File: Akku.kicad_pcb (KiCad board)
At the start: 2 copper layers, 100 x 160 mm, 49 parts, among them P1 CONN_02X10, P2 CONN_02X10, P3 CONN_02X10, P4 CONN_01X01, P5 CONN_01X01, P6 CONN_01X01, P7 CONN_01X01, P8 CONN_01X01, P9 CONN_01X01, SW1 SWITCH_INV, SW2 SWITCH_INV, SW3 SWITCH_INV, U1 7400, U2 7408, U3 74HC14, U4 74LS193, U5 74LS541, U6 74LS193, U7 74LS540, U8 74HC14

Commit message: Todo list dabei
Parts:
- removed REF**: EuroBoard160mmX100mm_holes, EuroBoard_Outline:EuroBoard160mmX100mm_holes
- added P10: CONN_01X01, Connect:1pin, F.Cu at (166.3, 60.7)
- added P11: CONN_01X01, Connect:1pin, F.Cu at (176.5, 60.7)
- P1, P2, P3: value CONN_02X10 -> CONN_01X01; footprint Connect:IDC_Header_Straight_20pins -> Connect:1pin
- P7, P8, P9: value CONN_01X01 -> CONN_02X10
- SW1: value SWITCH_INV -> UP_Bonsai_SWITCH_INV
- SW2: value SWITCH_INV -> DOWN_Bonsai_SWITCH_INV
- SW3: value SWITCH_INV -> CLR_Bonsai_SWITCH_INV
- U1: value 7400 -> 74HC14; footprint Housings_DIP:DIP-14_W7.62mm -> Housings_DIP:DIP-14_W7.62mm_LongPads
- U2: value 7408 -> 7400; footprint Housings_DIP:DIP-14_W7.62mm -> Housings_DIP:DIP-14_W7.62mm_LongPads
- U4: value 74LS193 -> 7408; footprint Housings_DIP:DIP-16_W7.62mm_LongPads -> Housings_DIP:DIP-14_W7.62mm_LongPads
- U5: value 74LS541 -> 74LS193; footprint Housings_DIP:DIP-20_W7.62mm_LongPads -> Housings_DIP:DIP-16_W7.62mm_LongPads
- U6: value 74LS193 -> 74LS541; footprint Housings_DIP:DIP-16_W7.62mm_LongPads -> Housings_DIP:DIP-20_W7.62mm_LongPads
- U7: value 74LS540 -> 74LS193; footprint Housings_DIP:DIP-20_W7.62mm_LongPads -> Housings_DIP:DIP-16_W7.62mm_LongPads
- U8: value 74HC14 -> 74LS540; footprint Housings_DIP:DIP-14_W7.62mm_LongPads -> Housings_DIP:DIP-20_W7.62mm_LongPads
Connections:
- D1 pad 1: GND -> Net-(D1-Pad1)
- D3 pad 1: Net-(D3-Pad1) -> GND
- P1 pad 1: GND -> enable
- P2 pad 1: GND -> up
- P3 pad 1: GND -> down
- P4 pad 1: down/up/enable/load/CLR -> CLR
- P6 pad 1: down/up/enable/load/CLR -> load
- P7 pad 1: down/up/enable/load/CLR -> Net-(P7-Pad1)
- P8 pad 1: down/up/enable/load/CLR -> Net-(P8-Pad1)
- P9 pad 1: down/up/enable/load/CLR -> GND
- R1 pad 2: Net-(R1-Pad2) -> up
- R10 pad 2: Net-(D1-Pad2) -> Net-(D2-Pad2)
- R11 pad 2: Net-(D2-Pad2) -> Net-(D3-Pad2)
- R5 pad 2: up -> Net-(R5-Pad2)
- R6 pad 1: VCC -> Net-(R6-Pad1)
- R6 pad 2: down -> VCC
- R9 pad 1: Net-(D3-Pad1) -> Net-(D1-Pad1)
- SW1 pad 1: Net-(SW1-Pad1) -> Net-(R4-Pad2)
- SW2 pad 1: Net-(R4-Pad2) -> Net-(R7-Pad2)
- U1 pad 1: Net-(R1-Pad2) -> enable
- U1 pad 10: Net-(R3-Pad1) -> (no net)
- U1 pad 11: Net-(U1-Pad11) -> (no net)
- U1 pad 12: Net-(R4-Pad2) -> (no net)
- U1 pad 13: Net-(U1-Pad13) -> (no net)
- U1 pad 4: Net-(U1-Pad4) -> Net-(R10-Pad1)
- U1 pad 5: Net-(R2-Pad2) -> Net-(U1-Pad5)
- U1 pad 6: Net-(U1-Pad6) -> Net-(D1-Pad2)
- U1 pad 8: Net-(U1-Pad13) -> Net-(R14-Pad1)
- U1 pad 9: Net-(U1-Pad11) -> load
- U2 pad 1: up -> Net-(R4-Pad2)
- U2 pad 10: (no net) -> Net-(R6-Pad1)
- U2 pad 12: Net-(U1-Pad13) -> Net-(R7-Pad2)
- U2 pad 13: down -> Net-(U2-Pad13)
- U2 pad 2: Net-(U1-Pad3) -> Net-(U2-Pad2)
- U2 pad 4: (no net) -> Net-(U2-Pad3)
- U2 pad 5: (no net) -> Net-(R5-Pad2)
- U2 pad 6: (no net) -> Net-(U2-Pad2)
- U2 pad 8: (no net) -> Net-(U2-Pad13)
- U2 pad 9: (no net) -> Net-(U2-Pad11)
- U3 pad 14: VDD -> VCC
- U3 pad 3: Net-(U3-Pad3) -> Net-(U1-Pad2)
- U3 pad 4: Net-(U3-Pad4) -> Net-(U1-Pad5)
- U3 pad 5: Net-(U2-Pad3) -> Net-(U3-Pad5)
- U3 pad 6: Net-(R10-Pad1) -> Net-(R11-Pad1)
- U3 pad 7: VSS -> GND
- U4 pad 1: Net-(U4-Pad1) -> up
- U4 pad 10: Net-(U4-Pad10) -> (no net)
- U4 pad 11: load -> Net-(U1-Pad3)
- U4 pad 12: Net-(U4-Pad12) -> Net-(U2-Pad13)
- U4 pad 13: Net-(U4-Pad13) -> down
- U4 pad 14: CLR -> VCC
- U4 pad 2: Net-(U4-Pad2) -> Net-(U2-Pad3)
- U4 pad 3: Net-(U4-Pad3) -> Net-(U3-Pad5)
- U4 pad 4: Net-(U2-Pad11) -> (no net)
- U4 pad 5: Net-(U4-Pad5) -> (no net)
- U4 pad 6: Net-(U4-Pad6) -> (no net)
- U4 pad 7: Net-(U4-Pad7) -> GND
- U4 pad 8: GND -> (no net)
- U4 pad 9: Net-(U4-Pad9) -> (no net)
- U5 pad 10: GND -> Net-(U5-Pad10)
- U5 pad 11: Net-(U5-Pad11) -> load
- U5 pad 14: Net-(U5-Pad14) -> CLR
- U5 pad 15: Net-(U4-Pad9) -> Net-(U5-Pad15)
- U5 pad 16: Net-(U4-Pad10) -> VCC
- U5 pad 2: Net-(U4-Pad2) -> Net-(U5-Pad2)
- U5 pad 3: Net-(U4-Pad3) -> Net-(U5-Pad3)
- U5 pad 4: Net-(U4-Pad7) -> Net-(U1-Pad3)
- U5 pad 5: Net-(U4-Pad6) -> Net-(U3-Pad5)
- U5 pad 8: Net-(U5-Pad8) -> GND
- U6 pad 1: Net-(U5-Pad13) -> Net-(U1-Pad5)
- U6 pad 10: Net-(U5-Pad12) -> GND
- U6 pad 11: load -> Net-(U6-Pad11)
- U6 pad 14: CLR -> Net-(U6-Pad14)
- U6 pad 15: Net-(U5-Pad14) -> Net-(U5-Pad9)
- U6 pad 16: VCC -> Net-(U5-Pad10)
- U6 pad 2: Net-(U5-Pad6) -> Net-(U5-Pad2)
- U6 pad 3: Net-(U5-Pad7) -> Net-(U5-Pad3)
- U6 pad 4: Net-(U4-Pad13) -> Net-(U5-Pad7)
- U6 pad 5: Net-(U4-Pad12) -> Net-(U5-Pad6)
- U6 pad 6: Net-(U5-Pad9) -> Net-(U6-Pad6)
- U6 pad 7: Net-(U5-Pad8) -> Net-(U6-Pad7)
- U6 pad 8: GND -> Net-(U6-Pad8)
- U6 pad 9: Net-(U5-Pad11) -> Net-(U6-Pad9)
- U7 pad 1: Net-(U7-Pad1) -> Net-(U6-Pad13)
- U7 pad 10: GND -> Net-(U6-Pad12)
- U7 pad 11: Net-(R21-Pad2) -> load
- U7 pad 12: Net-(R20-Pad2) -> Net-(U7-Pad12)
- U7 pad 13: Net-(R19-Pad2) -> Net-(U7-Pad13)
- U7 pad 14: Net-(R18-Pad2) -> CLR
- U7 pad 15: Net-(R17-Pad2) -> Net-(U6-Pad14)
- U7 pad 16: Net-(R16-Pad2) -> VCC
- U7 pad 2: Net-(U4-Pad2) -> Net-(U6-Pad6)
- U7 pad 3: Net-(U4-Pad3) -> Net-(U6-Pad7)
- U7 pad 4: Net-(U4-Pad7) -> Net-(U5-Pad13)
- U7 pad 5: Net-(U4-Pad6) -> Net-(U5-Pad12)
- U7 pad 6: Net-(U5-Pad6) -> Net-(U6-Pad9)
- U7 pad 7: Net-(U5-Pad7) -> Net-(U6-Pad8)
- U7 pad 8: Net-(U5-Pad8) -> GND
- U7 pad 9: Net-(U5-Pad9) -> Net-(U6-Pad11)
- U8 pad 1: enable -> GND
- U8 pad 10: (no net) -> GND
- U8 pad 11: (no net) -> Net-(R21-Pad2)
- U8 pad 12: (no net) -> Net-(R20-Pad2)
- U8 pad 13: (no net) -> Net-(R19-Pad2)
- U8 pad 14: VCC -> Net-(R18-Pad2)
- U8 pad 2: Net-(U3-Pad3) -> Net-(U5-Pad2)
- U8 pad 3: Net-(U2-Pad11) -> Net-(U5-Pad3)
- U8 pad 4: Net-(R11-Pad1) -> Net-(U5-Pad7)
- U8 pad 5: Net-(U3-Pad4) -> Net-(U5-Pad6)
- U8 pad 6: Net-(D3-Pad2) -> Net-(U6-Pad6)
- U8 pad 7: GND -> Net-(U6-Pad7)
- U8 pad 8: Net-(R14-Pad1) -> Net-(U6-Pad8)
- U8 pad 9: load -> Net-(U6-Pad9)
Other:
- board outline removed

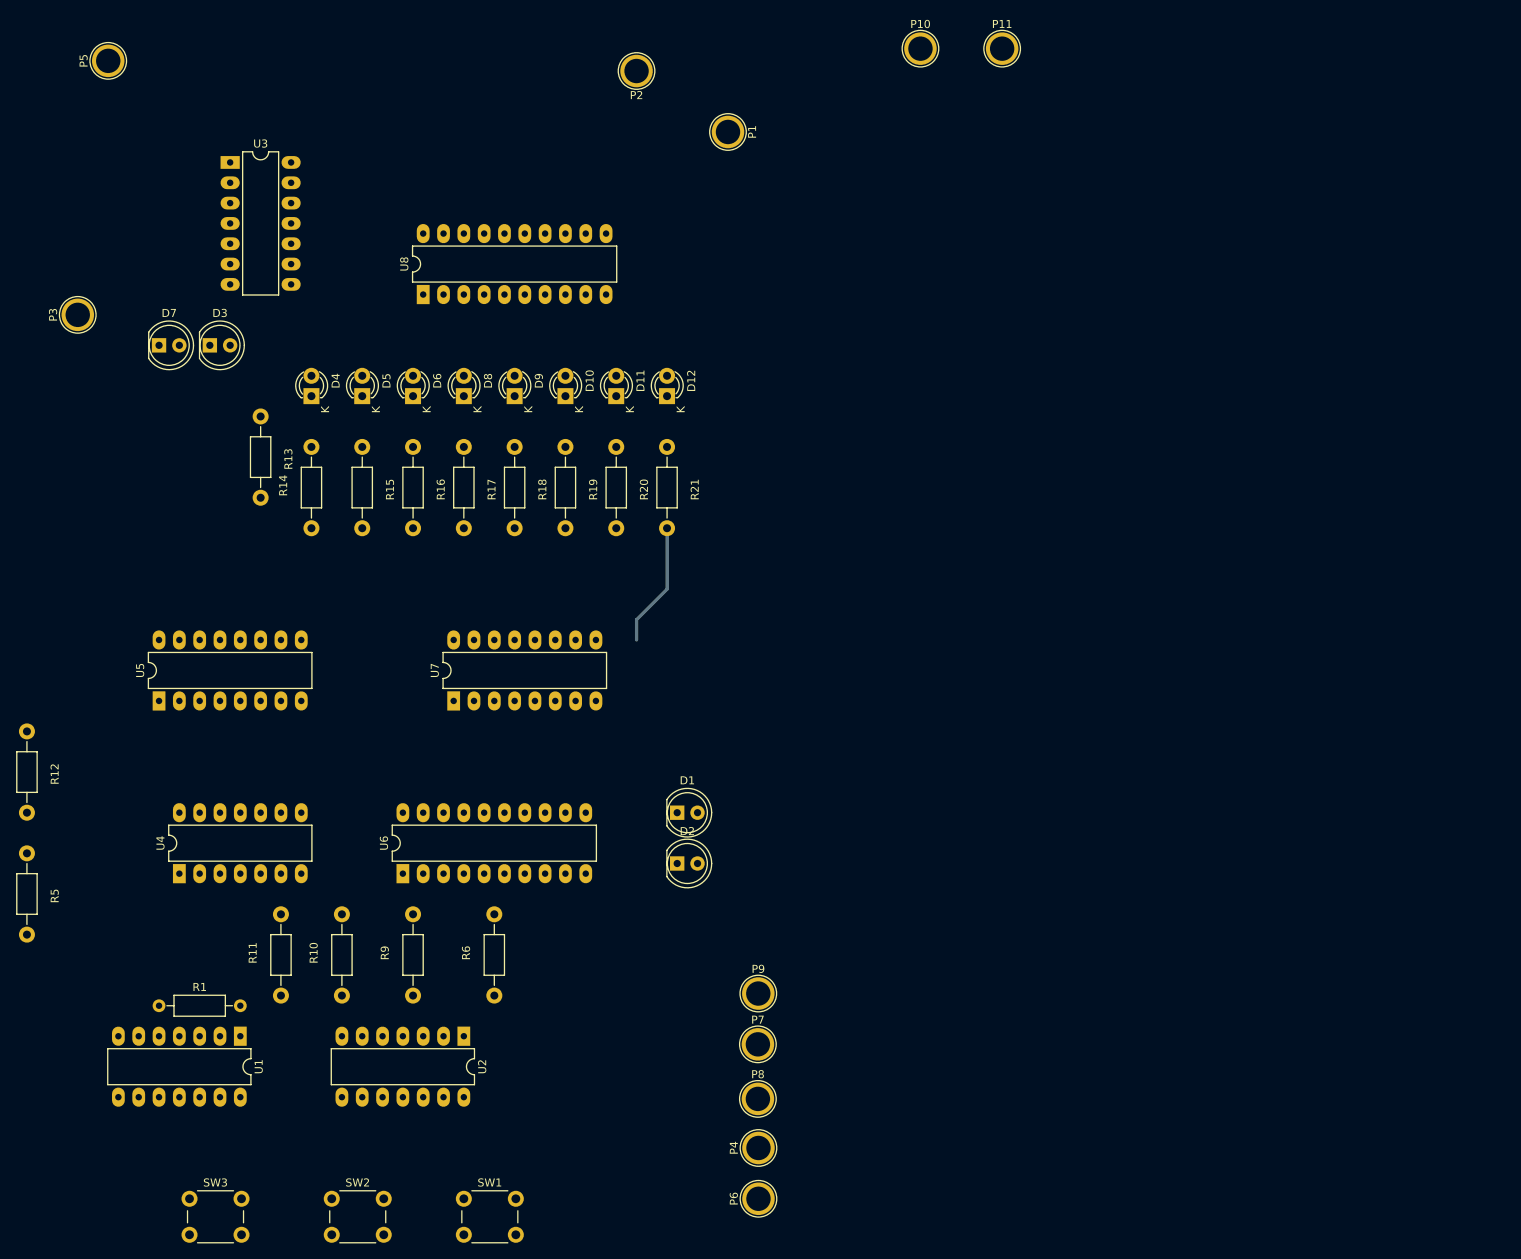
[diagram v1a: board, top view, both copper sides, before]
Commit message: R2-R22 ausgetauscht und Buttons (footprints), todolist anglegt, Bauteile angeordnet (80%)
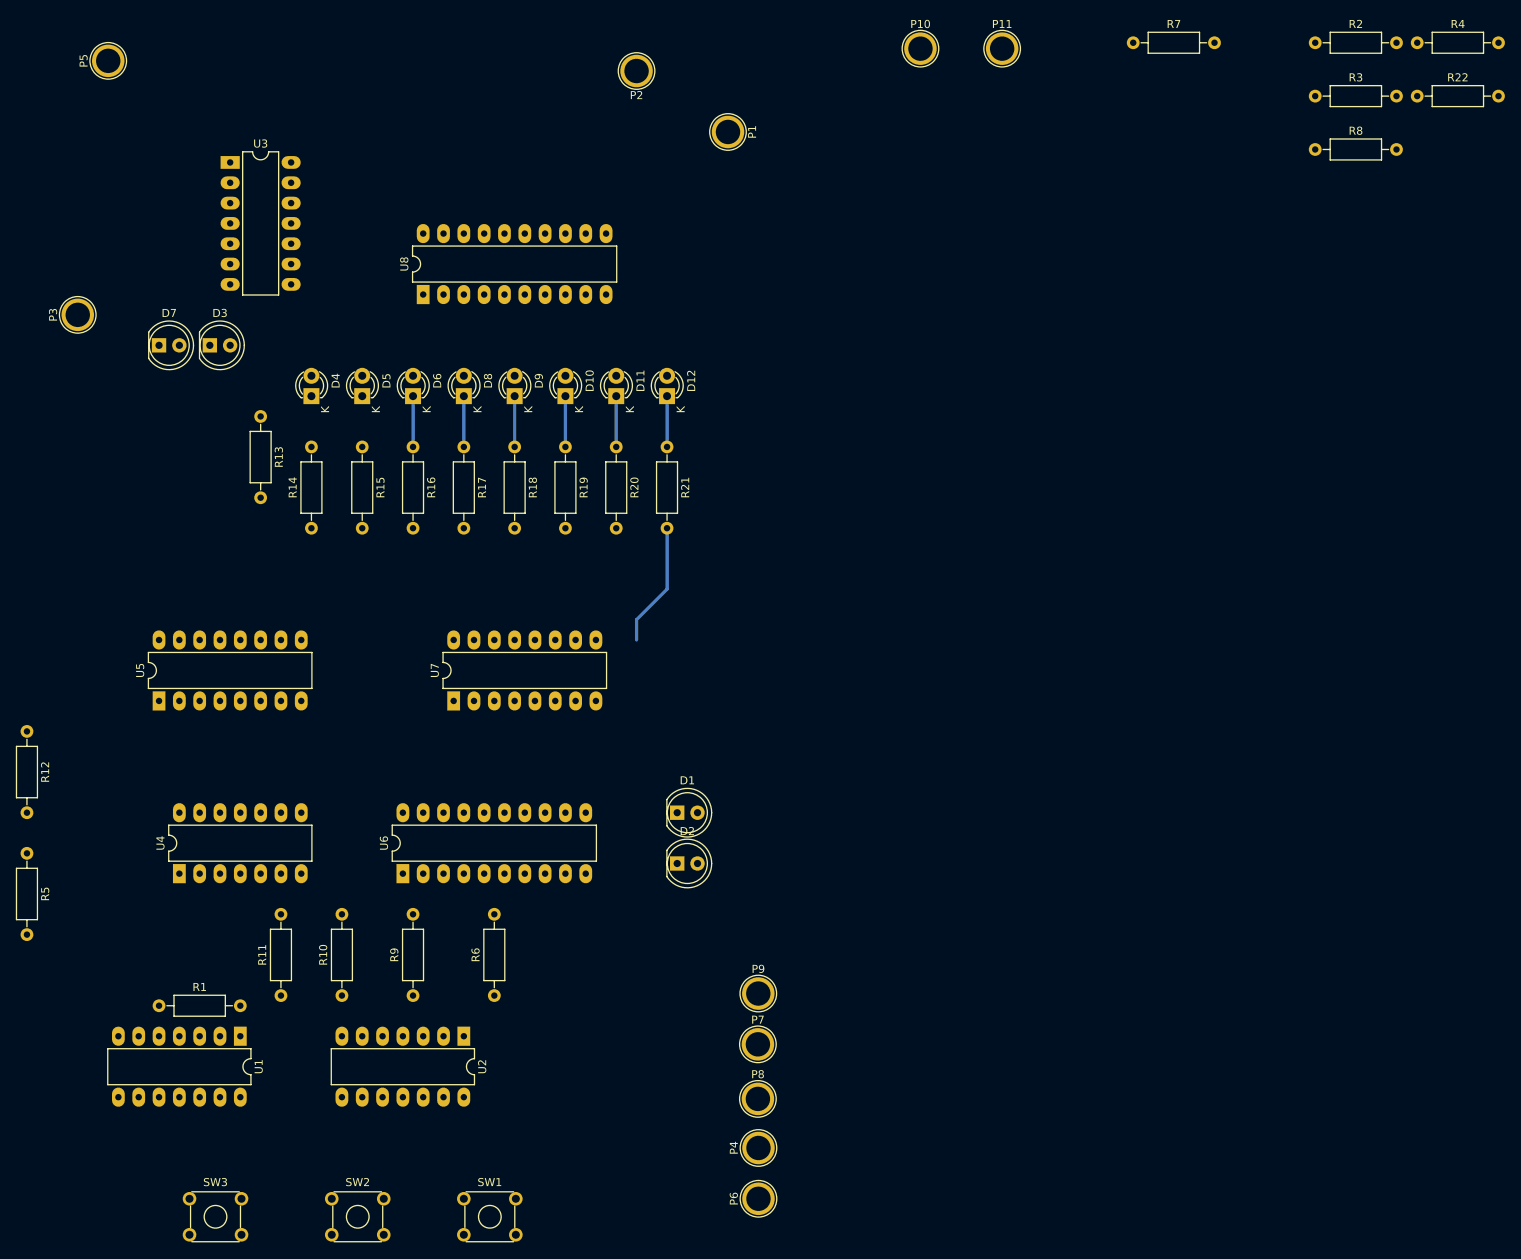
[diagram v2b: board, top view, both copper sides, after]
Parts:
- added R2: R, Resistors_ThroughHole:R_Axial_DIN0207_L6.3mm_D2.5mm_P10.16mm_Horizontal, F.Cu at (215.6, 60.0)
- added R22: R, Resistors_ThroughHole:R_Axial_DIN0207_L6.3mm_D2.5mm_P10.16mm_Horizontal, F.Cu at (228.4, 66.6)
- added R3: R, Resistors_ThroughHole:R_Axial_DIN0207_L6.3mm_D2.5mm_P10.16mm_Horizontal, F.Cu at (215.6, 66.6)
- added R4: R, Resistors_ThroughHole:R_Axial_DIN0207_L6.3mm_D2.5mm_P10.16mm_Horizontal, F.Cu at (228.4, 60.0)
- added R7: R, Resistors_ThroughHole:R_Axial_DIN0207_L6.3mm_D2.5mm_P10.16mm_Horizontal, F.Cu at (192.9, 60.0)
- added R8: R, Resistors_ThroughHole:R_Axial_DIN0207_L6.3mm_D2.5mm_P10.16mm_Horizontal, F.Cu at (215.6, 73.3)
- R10, R11, R12, R13, R14, R15, R16, R17, R18, R19, R20, R21, R5, R6, R9: footprint Resistors_ThroughHole:Resistor_Horizontal_RM10mm -> Resistors_ThroughHole:R_Axial_DIN0207_L6.3mm_D2.5mm_P10.16mm_Horizontal
- SW1, SW2, SW3: footprint Buttons_Switches_ThroughHole:SW_PUSH_6mm_h5mm -> Buttons_Switches_ThroughHole:SW_TH_Tactile_Omron_B3F-10xx
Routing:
- net Net-(D9-Pad1): track 0.00 -> 6.35 mm
- net Net-(D8-Pad1): track 0.00 -> 6.35 mm
- net Net-(D6-Pad1): track 0.00 -> 6.35 mm
- net Net-(D12-Pad1): track 0.00 -> 6.35 mm
- net Net-(D11-Pad1): track 0.00 -> 6.35 mm
- net Net-(D10-Pad1): track 0.00 -> 6.35 mm

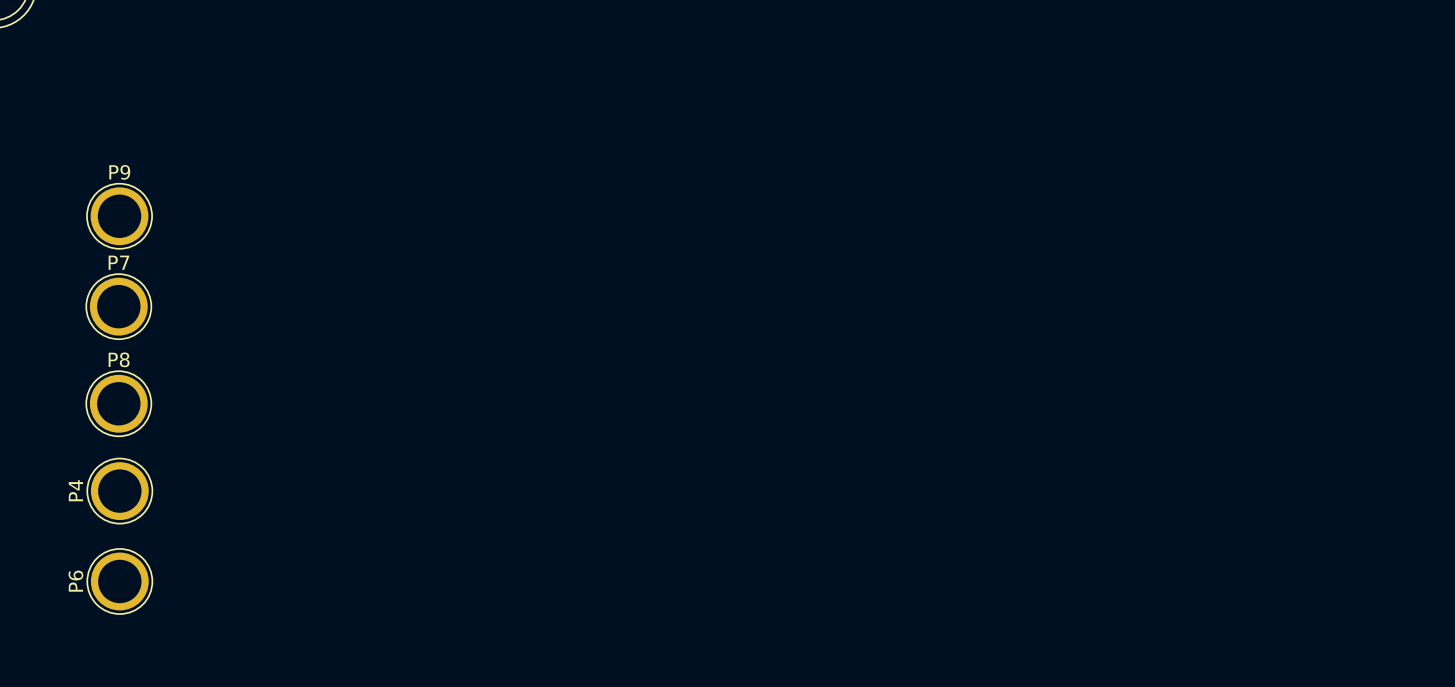
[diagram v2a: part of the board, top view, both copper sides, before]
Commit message: foodprint 2x10 Header size adjusted
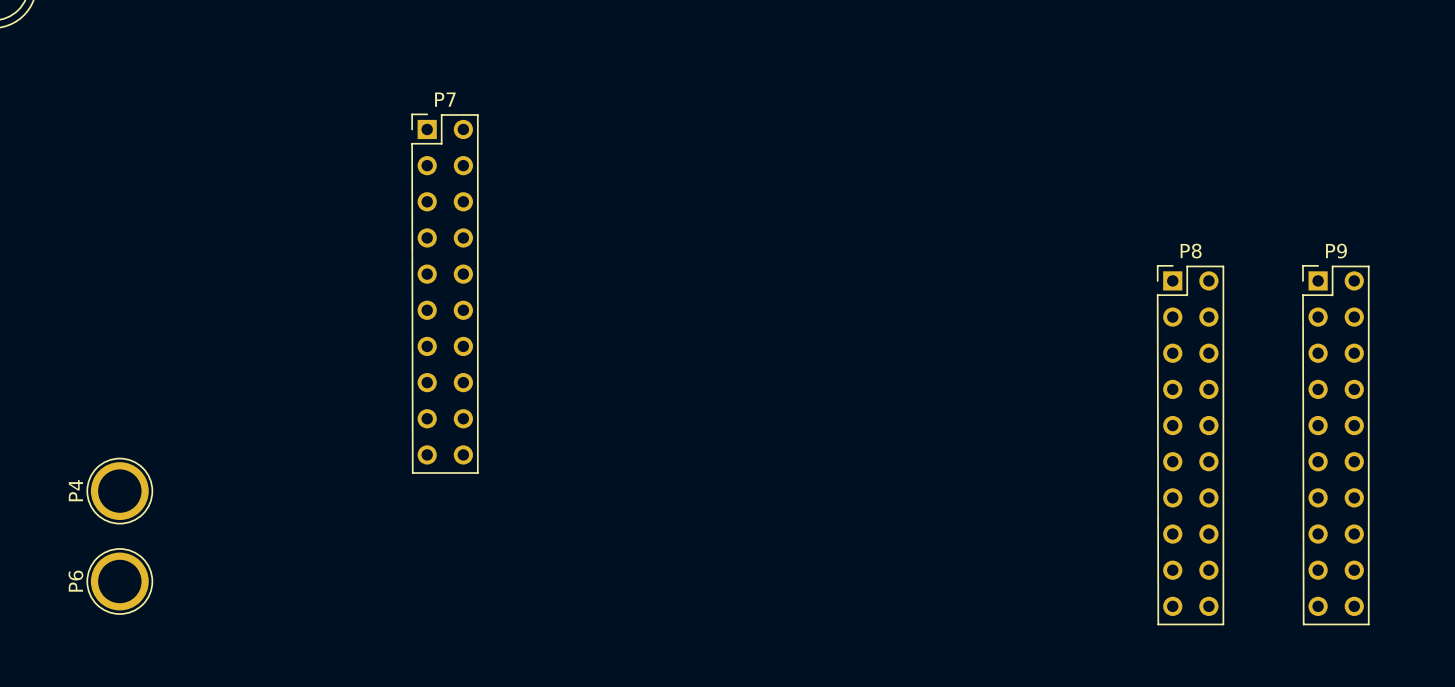
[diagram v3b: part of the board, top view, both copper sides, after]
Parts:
- P7, P8, P9: footprint Connect:1pin -> tg_foodprint:Pin_Header_Straight_2x10_Pitch2.00mmBonsai.pretty
- moved P9 84.3 mm to (230.2, 183.4)
- moved P8 74.5 mm to (220.0, 183.4)
- moved P7 25.0 mm to (167.6, 172.7)
